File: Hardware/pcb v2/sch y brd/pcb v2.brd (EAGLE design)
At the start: 80 x 80 mm, 58 parts, among them J1 AVR_SPI_PRG_6PTH, J2 1981584-1, J3 HDMI, J4 JST-3, J5 HDMI, Q1 PMBT3904, Q2 PMBT3904, Q3 MC-306, U1 ATMEGA328P, U2 TXS0108EPWR-TSSOP20, U3 ADP3338AKCZ-3.3RL7, U4 DS1307SO8, Y1 CSTCE16M0V53-R0 16MHZ

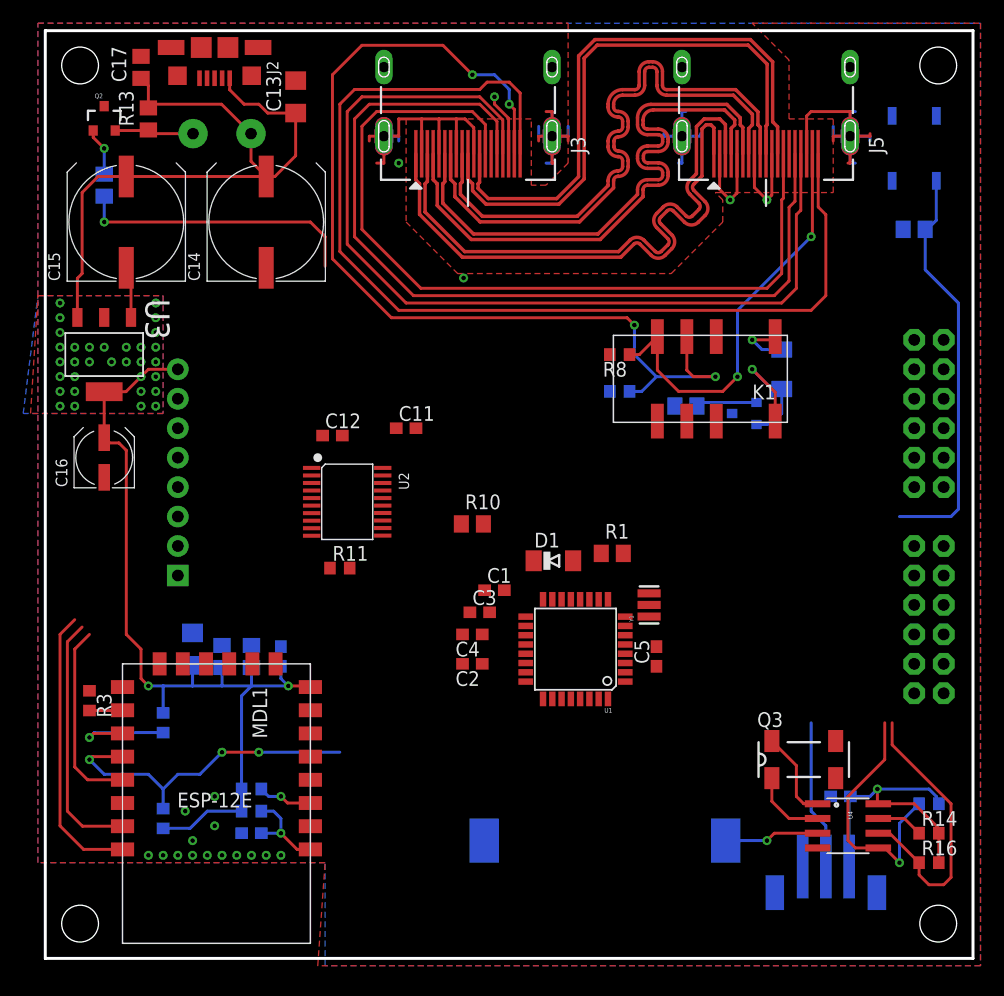
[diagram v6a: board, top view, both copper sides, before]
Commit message: ruteo completo
falta arreglar la serigrafia
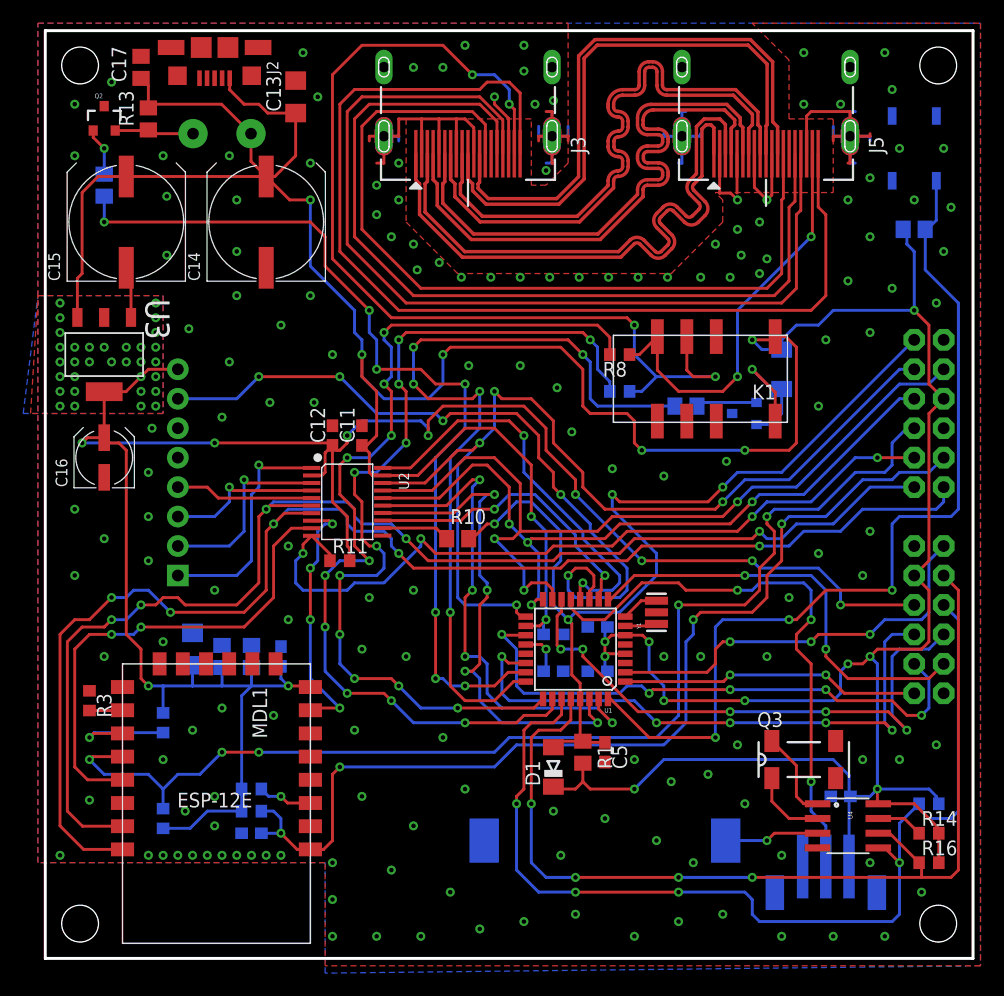
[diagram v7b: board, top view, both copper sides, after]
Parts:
- moved D1 17.8 mm to (43.8, 16.5), turned to 90 degrees
- moved R1 17.3 mm to (46.4, 17.8), turned to 270 degrees
- moved C2 10.8 mm to (47.6, 24.8), flipped to the bottom, turned to 0 degrees
- moved C1 9.44 mm to (47.6, 28.6), flipped to the bottom
- moved C5 9.38 mm to (48.3, 17.8), turned to 270 degrees
- moved C4 7.67 mm to (43.8, 24.8), flipped to the bottom
- moved C3 6.63 mm to (43.8, 27.9), flipped to the bottom, turned to 180 degrees
- moved C11 3.86 mm to (27.3, 45.1), turned to 90 degrees
- moved R10 1.80 mm to (35.6, 36.2)
- moved Y1 0.90 mm to (52.7, 29.8)
- moved R11 0.63 mm to (25.4, 34.3)
- turned C12 to 90 degrees
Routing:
- net +5V: track 89.0 -> 352.4 mm, vias 2 -> 18
- net +3V3: track 76.4 -> 178.7 mm, vias 34 -> 42
- net ESP_TX_3V3: track 24.5 -> 118.1 mm, vias 0 -> 5
- net ESP_RX_3V3: track 21.7 -> 111.5 mm, vias 0 -> 5
- net RST_ATM: track 0.00 -> 84.3 mm, vias 0 -> 4
- net N$17: track 0.00 -> 83.1 mm, vias 0 -> 4
- net N$37: track 0.00 -> 81.5 mm, vias 0 -> 10
- net ESP_OC_NRST: track 8.03 -> 87.8 mm, vias 1 -> 4
- net N$34: track 0.00 -> 77.6 mm, vias 0 -> 11
- net N$19: track 0.00 -> 72.2 mm, vias 0 -> 3
- net ESP_OC_NPROG: track 28.6 -> 100.3 mm, vias 3 -> 5
- net RELE: track 0.00 -> 70.9 mm, vias 0 -> 5
- net LVLSHF_OC_OE: track 0.00 -> 67.2 mm, vias 0 -> 4
- net SDA: track 22.5 -> 88.7 mm, vias 1 -> 4
- net N$18: track 0.00 -> 64.0 mm, vias 0 -> 4
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
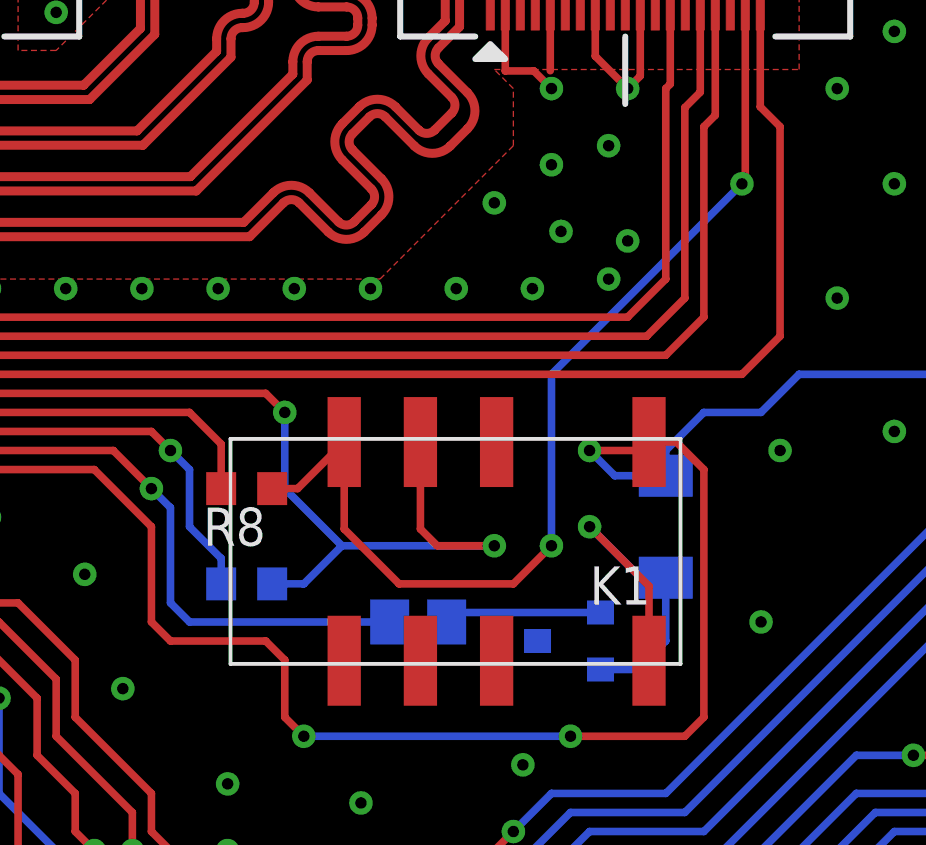
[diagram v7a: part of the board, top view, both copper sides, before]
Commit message: gerbers y render
falta arreglar la serigrafia
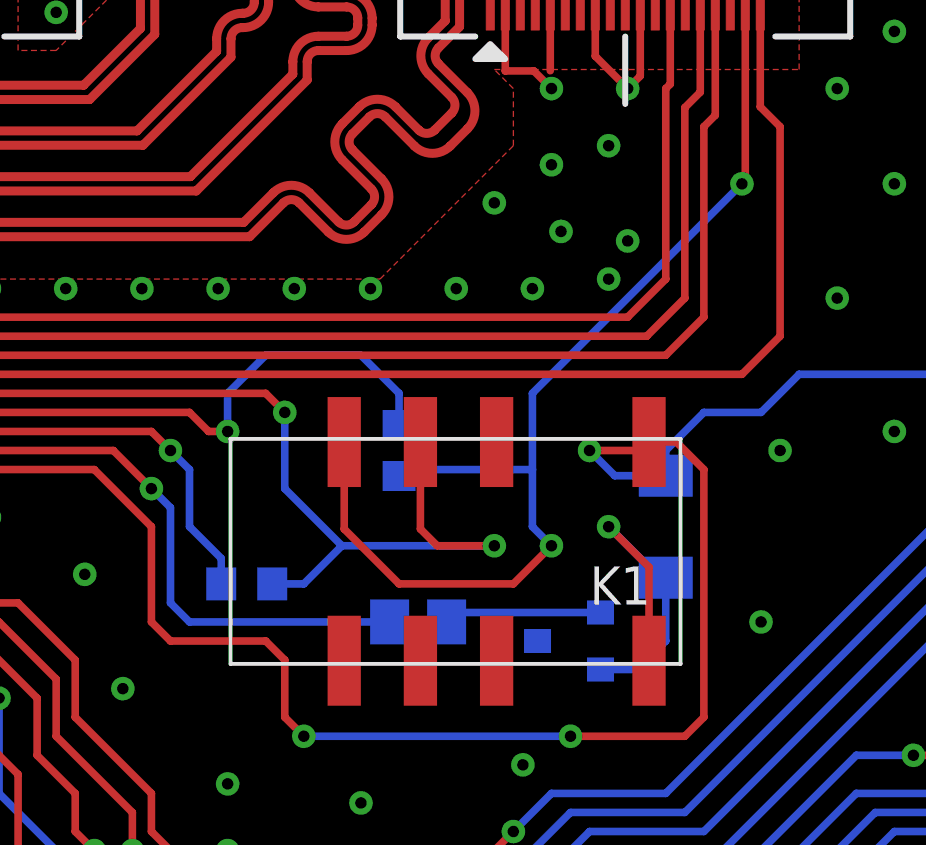
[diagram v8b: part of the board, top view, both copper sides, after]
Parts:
- moved R8 5.24 mm to (54.6, 53.3), flipped to the bottom, turned to 90 degrees
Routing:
- net N$37: track 81.5 -> 89.2 mm, vias 10 -> 11
- net HDMI_B_5V: track 36.0 -> 38.1 mm
- net N$15: track 13.2 -> 12.3 mm
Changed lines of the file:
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@@
 <layer number="20" name="Dimension" color="15" fill="1" visible="yes" active="yes"/>
 <layer number="21" name="tPlace" color="7" fill="1" visible="yes" active="yes"/>
-<layer number="22" name="bPlace" color="7" fill="1" visible="no" active="yes"/>
+<layer number="22" name="bPlace" color="7" fill="1" visible="yes" active="yes"/>
 <layer number="23" name="tOrigins" color="15" fill="1" visible="yes" active="yes"/>
-<layer number="24" name="bOrigins" color="15" fill="1" visible="no" active="yes"/>
+<layer number="24" name="bOrigins" color="15" fill="1" visible="yes" active="yes"/>
 <layer number="25" name="tNames" color="7" fill="1" visible="yes" active="yes"/>
-<layer number="26" name="bNames" color="7" fill="1" visible="no" active="yes"/>
+<layer number="26" name="bNames" color="7" fill="1" visible="yes" active="yes"/>
 <layer number="27" name="tValues" color="7" fill="1" visible="no" active="yes"/>
 <layer number="28" name="bValues" color="7" fill="1" visible="no" active="yes"/>
@@
 <layer number="50" name="dxf" color="7" fill="1" visible="no" active="no"/>
 <layer number="51" name="tDocu" color="7" fill="1" visible="yes" active="yes"/>
-<layer number="52" name="bDocu" color="7" fill="1" visible="no" active="yes"/>
+<layer number="52" name="bDocu" color="7" fill="1" visible="yes" active="yes"/>
 <layer number="53" name="tGND_GNDA" color="7" fill="9" visible="no" active="no"/>
 <layer number="54" name="bGND_GNDA" color="1" fill="9" visible="no" active="no"/>
@@
 <attribute name="OC_FARNELL" value="1319313" x="27.94" y="64.77" size="1.778" layer="27" rot="R270" display="off"/>
 </element>
-<element name="R8" library="rcl" package="R0603" value="10k" x="49.53" y="52.07" rot="R180"/>
+<element name="R8" library="rcl" package="R0603" value="10k" x="54.61" y="53.34" rot="MR90"/>
 <element name="S1" library="SparkFun-Electromechanical" package="TACTILE-SWITCH-SMD" value="SWITCH-MOMENTARY-2SMD" x="74.93" y="69.85" locked="yes" smashed="yes" rot="MR90">
 <attribute name="PROD_ID" value="SWCH-08247" x="74.93" y="69.85" size="1.778" layer="28" rot="MR90" display="off"/>
@@
 <contactref element="K1" pad="12"/>
 <contactref element="Q1" pad="2"/>
-<wire x1="63.5" y1="49.1" x2="62.66" y2="49.1" width="0.254" layer="16"/>
-<wire x1="62.66" y1="49.1" x2="60.96" y2="50.8" width="0.254" layer="16"/>
-<via x="60.96" y="50.8" extent="1-16" drill="0.381" diameter="0.7874"/>
-<wire x1="60.96" y1="50.8" x2="62.941265625" y2="48.818734375" width="0.254" layer="1"/>
-<wire x1="62.941265625" y1="48.818734375" x2="62.941265625" y2="46.332284375" width="0.254" layer="1"/>
+<via x="61.595" y="50.8" extent="1-16" drill="0.381" diameter="0.7874"/>
+<wire x1="61.595" y1="50.8" x2="62.941265625" y2="49.453734375" width="0.254" layer="1"/>
+<wire x1="62.941265625" y1="49.453734375" x2="62.941265625" y2="46.332284375" width="0.254" layer="1"/>
 <wire x1="61.325" y1="46.04" x2="62.55" y2="46.04" width="0.254" layer="16"/>
 <wire x1="62.55" y1="46.04" x2="63.5" y2="46.99" width="0.254" layer="16"/>
 <wire x1="63.5" y1="46.99" x2="63.5" y2="49.1" width="0.254" layer="16"/>
+<wire x1="61.595" y1="50.8" x2="63.295" y2="49.1" width="0.254" layer="16"/>
+<wire x1="63.295" y1="49.1" x2="63.5" y2="49.1" width="0.254" layer="16"/>
 </signal>
 <signal name="N$20">
@@
 <wire x1="58.42" y1="48.895" x2="59.69" y2="50.165" width="0.254" layer="1"/>
 <via x="59.69" y="50.165" extent="1-16" drill="0.381" diameter="0.7874"/>
-<wire x1="59.69" y1="50.165" x2="59.69" y2="55.88" width="0.254" layer="16"/>
-<wire x1="59.69" y1="55.88" x2="66.04" y2="62.23" width="0.254" layer="16"/>
+<wire x1="59.69" y1="50.165" x2="59.055" y2="50.8" width="0.254" layer="16"/>
+<wire x1="59.055" y1="50.8" x2="59.055" y2="52.705" width="0.254" layer="16"/>
+<wire x1="59.055" y1="52.705" x2="59.055" y2="55.245" width="0.254" layer="16"/>
+<wire x1="59.055" y1="55.245" x2="66.04" y2="62.23" width="0.254" layer="16"/>
 <via x="66.04" y="62.23" extent="1-16" drill="0.381" diameter="0.7874"/>
 <wire x1="66.04" y1="62.23" x2="66.15" y2="62.34" width="0.254" layer="1"/>
 <wire x1="66.15" y1="62.34" x2="66.15" y2="69.39" width="0.254" layer="1"/>
-<wire x1="50.38" y1="52.07" x2="51.22898125" y2="52.07" width="0.254" layer="1"/>
-<wire x1="51.22898125" y1="52.07" x2="52.781265625" y2="53.622284375" width="0.254" layer="1"/>
+<wire x1="54.61" y1="52.49" x2="54.825" y2="52.705" width="0.254" layer="16"/>
+<wire x1="54.825" y1="52.705" x2="59.055" y2="52.705" width="0.254" layer="16"/>
 </signal>
 <signal name="N$34">
@@
 <wire x1="41.275" y1="20.955" x2="40.64" y2="20.32" width="0.254" layer="1"/>
 <wire x1="40.64" y1="20.32" x2="36.195" y2="20.32" width="0.254" layer="1"/>
-<wire x1="48.68" y1="52.07" x2="48.68" y2="53.555" width="0.254" layer="1"/>
-<wire x1="48.68" y1="53.555" x2="47.625" y2="54.61" width="0.254" layer="1"/>
 <wire x1="47.625" y1="54.61" x2="29.845" y2="54.61" width="0.254" layer="1"/>
 <wire x1="29.845" y1="54.61" x2="29.21" y2="53.975" width="0.254" layer="1"/>
@@
 <via x="24.13" y="28.575" extent="1-16" drill="0.381" diameter="0.7874"/>
 <wire x1="24.13" y1="28.575" x2="24.13" y2="24.765" width="0.254" layer="16"/>
+<wire x1="47.625" y1="54.61" x2="48.26" y2="53.975" width="0.254" layer="1"/>
+<wire x1="48.26" y1="53.975" x2="48.895" y2="53.975" width="0.254" layer="1"/>
+<via x="48.895" y="53.975" extent="1-16" drill="0.381" diameter="0.7874"/>
+<wire x1="48.895" y1="53.975" x2="48.895" y2="55.245" width="0.254" layer="16"/>
+<wire x1="48.895" y1="55.245" x2="50.165" y2="56.515" width="0.254" layer="16"/>
+<wire x1="50.165" y1="56.515" x2="53.34" y2="56.515" width="0.254" layer="16"/>
+<wire x1="53.34" y1="56.515" x2="54.61" y2="55.245" width="0.254" layer="16"/>
+<wire x1="54.61" y1="55.245" x2="54.61" y2="54.19" width="0.254" layer="16"/>
 </signal>
 <signal name="N$41">
